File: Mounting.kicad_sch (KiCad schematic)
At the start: 4 parts

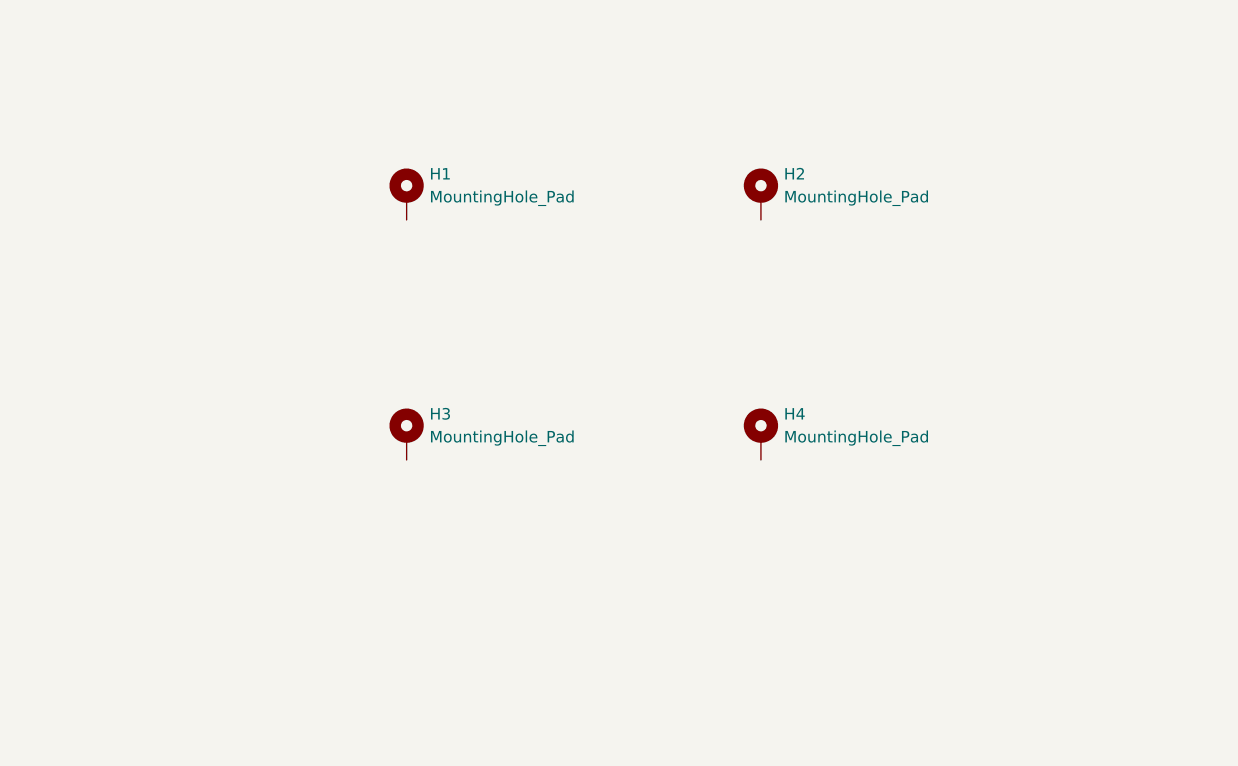
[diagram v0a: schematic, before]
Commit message: 2026 08 16 原理图完成，下一步制作分配未完成的器件封装，准备layout
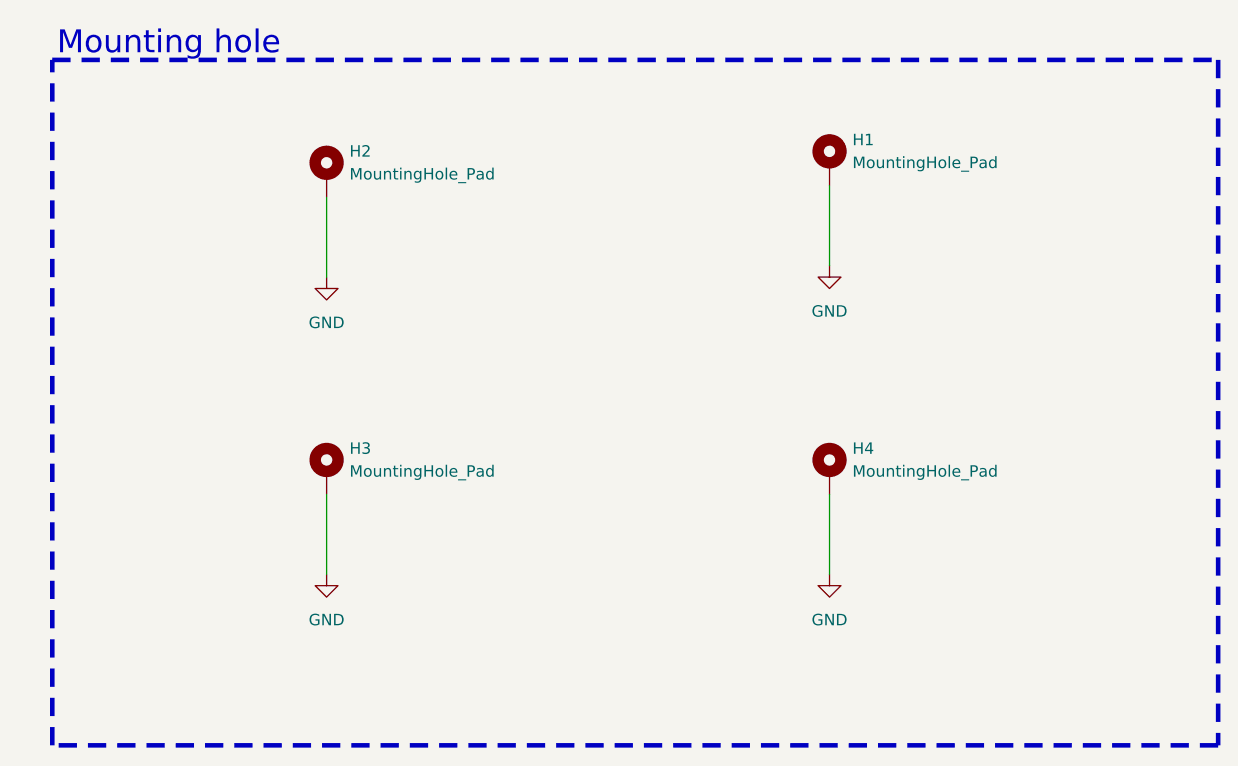
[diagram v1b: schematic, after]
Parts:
- renumbered H2 to H1, H1 to H2
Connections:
- net GND: now reaches H1.1
- net GND: now also H2.1, H3.1, H4.1
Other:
- note added: "Mounting hole"
- moved on the sheet: H1, H2, H3, H4

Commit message: 2026 08 24 画图完成，准备生产
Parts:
- H1, H2, H3, H4: footprint MountingHole:MountingHole_2.2mm_M2_ISO7380_Pad -> MountingHole:MountingHole_3.2mm_M3_Pad_Via
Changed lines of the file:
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@@
 			)
 		)
-		(property "Footprint" "MountingHole:MountingHole_2.2mm_M2_ISO7380_Pad"
+		(property "Footprint" "MountingHole:MountingHole_3.2mm_M3_Pad_Via"
 			(at 167.64 69.85 0)
 			(hide yes)
@@
 			)
 		)
-		(property "Footprint" "MountingHole:MountingHole_2.2mm_M2_ISO7380_Pad"
+		(property "Footprint" "MountingHole:MountingHole_3.2mm_M3_Pad_Via"
 			(at 111.76 104.14 0)
 			(hide yes)
@@
 			)
 		)
-		(property "Footprint" "MountingHole:MountingHole_2.2mm_M2_ISO7380_Pad"
+		(property "Footprint" "MountingHole:MountingHole_3.2mm_M3_Pad_Via"
 			(at 111.76 71.12 0)
 			(hide yes)
@@
 			)
 		)
-		(property "Footprint" "MountingHole:MountingHole_2.2mm_M2_ISO7380_Pad"
+		(property "Footprint" "MountingHole:MountingHole_3.2mm_M3_Pad_Via"
 			(at 167.64 104.14 0)
 			(hide yes)
